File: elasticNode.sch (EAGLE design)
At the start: 113 parts, among them J1 ISP_CONN_6PIN, J10 ISP_CONN_6PIN, J2 FEMALE_HEADER_2X2, J3 FEMALE_HEADER_2X1, J4 FEMALE_HEADER_2X1, J5 FEMALE_HEADER_10X2, J8 USB_CONNSMT, J9 USB_CONNSMT, U1 ATMEGA64AQFN, U10 LTC3419DFN, U11 ATMEGA32U4, U2 SST26VF032B, U3 MRF24J40MA, U4 SPARTAN6-LX9, U5 SST26VF032B, U6 PAC1720, U7 PAC1720, U8 PAC1720, U9 FT232RSSOP28, X1 12MHz, X2 50MHz, X3 32MHz, X4 12MHz

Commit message: New layout is done
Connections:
- removed net N$33: U1.PB5_OC1A
- net 3V3: no longer R25.2
- net MCU_GPIO_0: now also J2.1, U1.PB7_OC2/OC1C; no longer J2.4, U1.PB6_OC1B
- net MCU_GPIO_1: now also J2.2, U1.PG3_TOSC2; no longer J2.3, U1.PE4_OC3B/INT4
- net MCU_GPIO_2: now also J2.3, U1.PG4_TOSC2; no longer J2.2, U1.PB7_OC2/OC1C
- net MCU_GPIO_3: now also J2.4, U1.PB6_OC1B; no longer J2.1, U1.PF0_ADC0
- net MCU_LED1: no longer U1.PB0_SS#
- net MCU_LED2: no longer U1.PE2_XCK0/AIN0
- net MCU_LED3: no longer U1.PE3_OC3A/AIN1
- net SDA: now also R25.2; no longer R25.1
- net WIRELESS_INT: now also U1.PF0_ADC0; no longer U1.PE7_ICP3/INT7
- net WIRELESS_RESET: now also U1.PB5_OC1A; no longer U1.PE5_OC3C/INT5
- net WIRELESS_WAKE: now also U1.PE2_XCK0/AIN0; no longer U1.PE6_T3/INT6
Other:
- moved on the sheet: R25
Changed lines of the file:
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@@
 <setting verticaltext="up"/>
 </settings>
-<grid distance="0.5" unitdist="mm" unit="mm" style="lines" multiple="1" display="yes" altdistance="0.01" altunitdist="inch" altunit="inch"/>
+<grid distance="1" unitdist="mm" unit="mm" style="lines" multiple="1" display="yes" altdistance="0.01" altunitdist="inch" altunit="inch"/>
 <layers>
 <layer number="1" name="Top" color="4" fill="1" visible="no" active="no"/>
@@
 </segment>
 <segment>
-<pinref part="U1" gate="G$1" pin="PE5_OC3C/INT5"/>
-<wire x1="7" y1="42" x2="7" y2="52" width="0.1524" layer="91"/>
-<label x="7" y="52" size="1.778" layer="95" rot="R90"/>
+<pinref part="U1" gate="G$1" pin="PB5_OC1A"/>
+<wire x1="-42" y1="-16" x2="-54" y2="-16" width="0.1524" layer="91"/>
+<label x="-54" y="-16" size="1.778" layer="95" rot="R180"/>
 </segment>
 </net>
@@
 </segment>
 <segment>
-<pinref part="U1" gate="G$1" pin="PE6_T3/INT6"/>
-<wire x1="4" y1="42" x2="4" y2="52" width="0.1524" layer="91"/>
-<label x="4" y="52" size="1.778" layer="95" rot="R90"/>
+<pinref part="U1" gate="G$1" pin="PE2_XCK0/AIN0"/>
+<wire x1="16" y1="52" x2="16" y2="42" width="0.1524" layer="91"/>
+<label x="16" y="52" size="1.778" layer="95" rot="R90"/>
 </segment>
 </net>
@@
 </segment>
 <segment>
-<pinref part="U1" gate="G$1" pin="PE7_ICP3/INT7"/>
-<wire x1="1" y1="42" x2="1" y2="52" width="0.1524" layer="91"/>
-<label x="1" y="52" size="1.778" layer="95" rot="R90"/>
+<pinref part="U1" gate="G$1" pin="PF0_ADC0"/>
+<wire x1="-2" y1="42" x2="-2" y2="52" width="0.1524" layer="91"/>
+<label x="-2" y="52" size="1.778" layer="95" rot="R90"/>
 </segment>
 </net>
@@
 <net name="MCU_GPIO_0" class="0">
 <segment>
+<pinref part="J2" gate="G$1" pin="1"/>
+<wire x1="134" y1="21.5" x2="122" y2="21.5" width="0.1524" layer="91"/>
+<label x="122" y="21.5" size="1.778" layer="95" rot="R180"/>
+</segment>
+<segment>
+<pinref part="U1" gate="G$1" pin="PB7_OC2/OC1C"/>
+<wire x1="-42" y1="-22" x2="-54" y2="-22" width="0.1524" layer="91"/>
+<label x="-54" y="-22" size="1.778" layer="95" rot="R180"/>
+</segment>
+</net>
+<net name="MCU_GPIO_1" class="0">
+<segment>
+<pinref part="J2" gate="G$1" pin="2"/>
+<wire x1="134" y1="18.5" x2="122" y2="18.5" width="0.1524" layer="91"/>
+<label x="122" y="18.5" size="1.778" layer="95" rot="R180"/>
+</segment>
+<segment>
+<pinref part="U1" gate="G$1" pin="PG3_TOSC2"/>
+<wire x1="54" y1="-13" x2="42" y2="-13" width="0.1524" layer="91"/>
+<label x="54" y="-13" size="1.778" layer="95"/>
+</segment>
+</net>
+<net name="MCU_GPIO_2" class="0">
+<segment>
+<pinref part="J2" gate="G$1" pin="3"/>
+<wire x1="154" y1="18.5" x2="165.5" y2="18.5" width="0.1524" layer="91"/>
+<label x="165.5" y="18.5" size="1.778" layer="95"/>
+</segment>
+<segment>
+<pinref part="U1" gate="G$1" pin="PG4_TOSC2"/>
+<wire x1="42" y1="-10" x2="54" y2="-10" width="0.1524" layer="91"/>
+<label x="54" y="-10" size="1.778" layer="95"/>
+</segment>
+</net>
+<net name="MCU_GPIO_3" class="0">
+<segment>
 <pinref part="J2" gate="G$1" pin="4"/>
 <wire x1="154" y1="21.5" x2="165.5" y2="21.5" width="0.1524" layer="91"/>
@@
 </segment>
 </net>
-<net name="MCU_GPIO_1" class="0">
-<segment>
-<pinref part="J2" gate="G$1" pin="3"/>
-<wire x1="154" y1="18.5" x2="165.5" y2="18.5" width="0.1524" layer="91"/>
-<label x="165.5" y="18.5" size="1.778" layer="95"/>
-</segment>
-<segment>
-<pinref part="U1" gate="G$1" pin="PE4_OC3B/INT4"/>
-<wire x1="10" y1="42" x2="10" y2="52" width="0.1524" layer="91"/>
-<label x="10" y="52" size="1.778" layer="95" rot="R90"/>
-</segment>
-</net>
-<net name="MCU_GPIO_2" class="0">
-<segment>
-<pinref part="J2" gate="G$1" pin="2"/>
-<wire x1="134" y1="18.5" x2="122" y2="18.5" width="0.1524" layer="91"/>
-<label x="122" y="18.5" size="1.778" layer="95" rot="R180"/>
-</segment>
-<segment>
-<pinref part="U1" gate="G$1" pin="PB7_OC2/OC1C"/>
-<wire x1="-42" y1="-22" x2="-54" y2="-22" width="0.1524" layer="91"/>
-<label x="-54" y="-22" size="1.778" layer="95" rot="R180"/>
-</segment>
-</net>
-<net name="MCU_GPIO_3" class="0">
-<segment>
-<pinref part="U1" gate="G$1" pin="PF0_ADC0"/>
-<wire x1="-2" y1="42" x2="-2" y2="52" width="0.1524" layer="91"/>
-<label x="-2" y="52" size="1.778" layer="95" rot="R90"/>
-</segment>
-<segment>
-<pinref part="J2" gate="G$1" pin="1"/>
-<wire x1="134" y1="21.5" x2="122" y2="21.5" width="0.1524" layer="91"/>
-<label x="122" y="21.5" size="1.778" layer="95" rot="R180"/>
-</segment>
-</net>
 <net name="N$13" class="0">
 <segment>
@@
 </segment>
 <segment>
-<pinref part="U1" gate="G$1" pin="PB0_SS#"/>
-<wire x1="-42" y1="-1" x2="-54" y2="-1" width="0.1524" layer="91"/>
-<label x="-54" y="-1" size="1.778" layer="95" rot="R180"/>
-</segment>
-<segment>
 <pinref part="U1" gate="G$1" pin="PD6_T1"/>
 <wire x1="19" y1="-40" x2="19" y2="-50" width="0.1524" layer="91"/>
@@
 </segment>
 <segment>
-<pinref part="U1" gate="G$1" pin="PE2_XCK0/AIN0"/>
-<wire x1="16" y1="52" x2="16" y2="42" width="0.1524" layer="91"/>
-<label x="16" y="52" size="1.778" layer="95" rot="R90"/>
-</segment>
-<segment>
 <pinref part="U1" gate="G$1" pin="PD5_XCK1"/>
 <wire x1="16" y1="-40" x2="16" y2="-50" width="0.1524" layer="91"/>
@@
 <wire x1="138.54" y1="-17" x2="129" y2="-17" width="0.1524" layer="91"/>
 <label x="129" y="-17" size="1.778" layer="95" rot="R180"/>
-</segment>
-<segment>
-<pinref part="U1" gate="G$1" pin="PE3_OC3A/AIN1"/>
-<wire x1="13" y1="42" x2="13" y2="52" width="0.1524" layer="91"/>
-<label x="13" y="52" size="1.778" layer="95" rot="R90"/>
 </segment>
 <segment>
@@
 <wire x1="42" y1="-16" x2="54" y2="-16" width="0.1524" layer="91"/>
 <label x="54" y="-16" size="1.778" layer="95"/>
-</segment>
-</net>
-<net name="N$33" class="0">
-<segment>
-<pinref part="U1" gate="G$1" pin="PB5_OC1A"/>
-<wire x1="-42" y1="-16" x2="-54" y2="-16" width="0.1524" layer="91"/>
-<label x="-54" y="-16" size="1.778" layer="95" rot="R180"/>
 </segment>
 </net>
@@
 <instance part="R22" gate="G$1" x="-40" y="-105" rot="R90"/>
 <instance part="R24" gate="G$1" x="26" y="-94.5" rot="R90"/>
-<instance part="R25" gate="G$1" x="26" y="-112.5" rot="R270"/>
+<instance part="R25" gate="G$1" x="26" y="-112.5" rot="R90"/>
 <instance part="U6" gate="G$1" x="-1" y="-52"/>
 <instance part="R20" gate="G$1" x="21" y="-67" rot="R90"/>
@@
 </segment>
 <segment>
-<pinref part="R25" gate="G$1" pin="2"/>
+<label x="26" y="-129" size="1.778" layer="95" rot="R270"/>
 <wire x1="26" y1="-116.96" x2="26" y2="-129" width="0.1524" layer="91"/>
-<label x="26" y="-129" size="1.778" layer="95" rot="R270"/>
 </segment>
 <segment>
@@
 <wire x1="16" y1="-107" x2="26" y2="-107" width="0.1524" layer="91"/>
 <label x="30" y="-107" size="1.778" layer="95"/>
-<pinref part="R25" gate="G$1" pin="1"/>
+<pinref part="R25" gate="G$1" pin="2"/>
 <wire x1="26" y1="-107" x2="30" y2="-107" width="0.1524" layer="91"/>
-<wire x1="26" y1="-108.04" x2="26" y2="-107" width="0.1524" layer="91"/>
+<wire x1="26" y1="-107" x2="26" y2="-108.04" width="0.1524" layer="91"/>
 <junction x="26" y="-107"/>
 </segment>

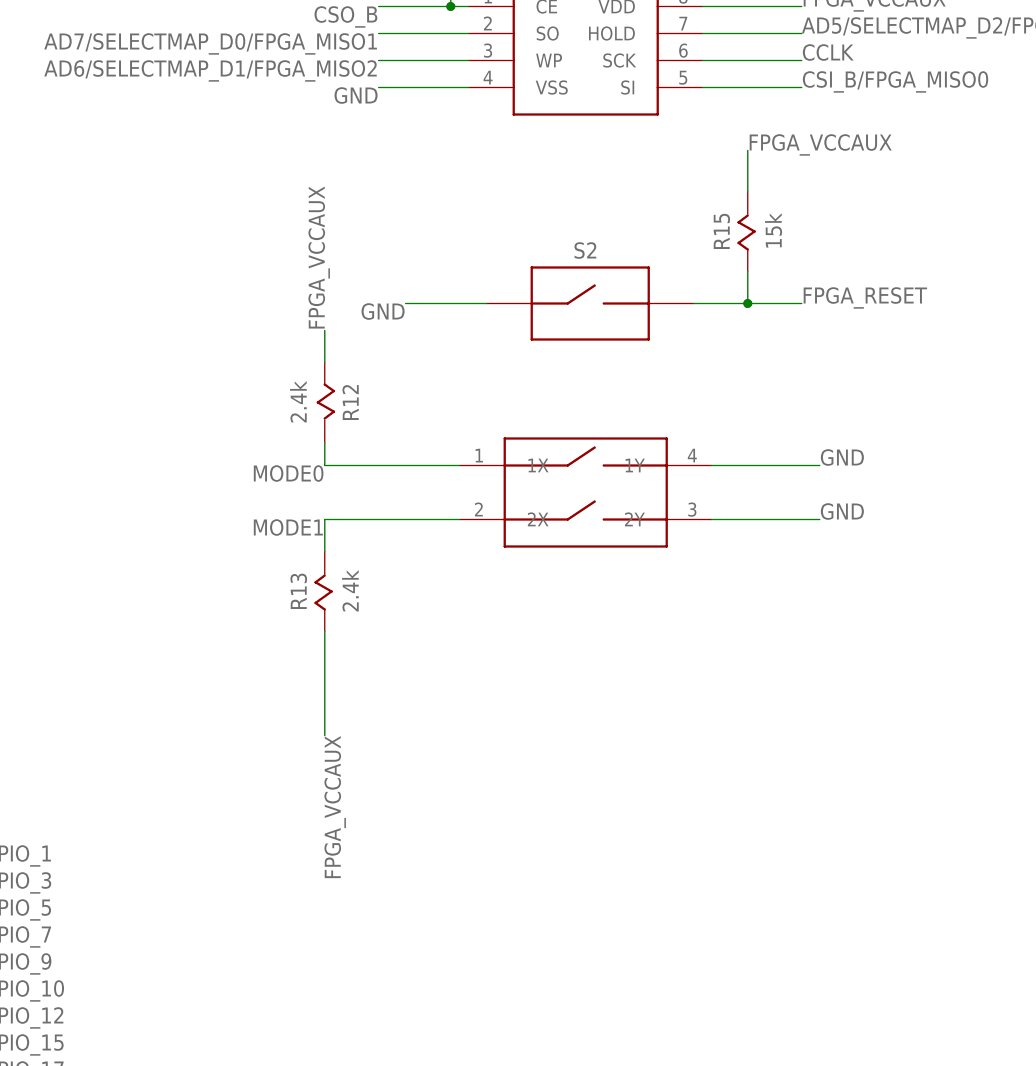
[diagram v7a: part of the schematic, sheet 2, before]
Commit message: 4-switch dip added into design
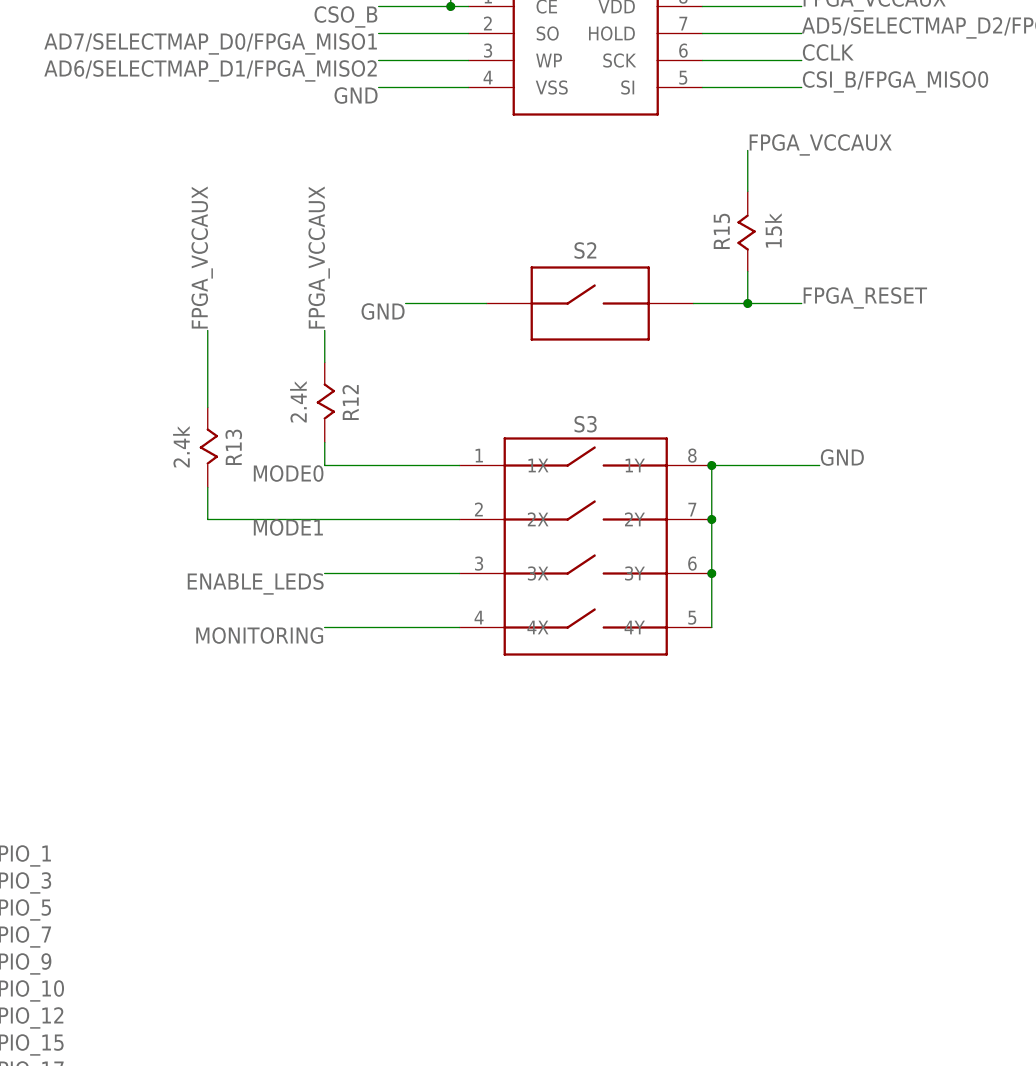
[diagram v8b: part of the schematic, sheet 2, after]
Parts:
- S3: value SPST_DIP_2SMT -> SPST_DIP_4; device connectors:SPST_DIP_2SMT -> connectors:SPST_DIP_4
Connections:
- new net ENABLE_LEDS: S3.3X, U1.PE7_ICP3/INT7
- new net MONITORING: S3.4X, U11.PE6(INT6/AIN0)
- net GND: now also S3.3Y, S3.4Y
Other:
- moved on the sheet: R13
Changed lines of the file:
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@@
 <attribute name="SPICEPREFIX" value="X"/>
 </part>
-<part name="S3" library="connectors" deviceset="SPST_DIP_2" device="SMT"/>
 <part name="R12" library="passive" deviceset="RESISTOR" device="" value="2.4k"/>
 <part name="R13" library="passive" deviceset="RESISTOR" device="" value="2.4k"/>
@@
 <part name="R36" library="passive" deviceset="RESISTOR" device="" value=".8"/>
 <part name="J5" library="connectors" deviceset="FEMALE_HEADER_10X2" device=""/>
+<part name="S3" library="connectors" deviceset="SPST_DIP_4" device=""/>
 </parts>
 <sheets>
@@
 <wire x1="42" y1="-16" x2="54" y2="-16" width="0.1524" layer="91"/>
 <label x="54" y="-16" size="1.778" layer="95"/>
+</segment>
+</net>
+<net name="ENABLE_LEDS" class="0">
+<segment>
+<pinref part="U1" gate="G$1" pin="PE7_ICP3/INT7"/>
+<wire x1="1" y1="42" x2="1" y2="52" width="0.1524" layer="91"/>
+<label x="1" y="52" size="1.778" layer="95" rot="R90"/>
 </segment>
 </net>
@@
 <instance part="S2" gate="G$1" x="197" y="-82"/>
 <instance part="R15" gate="G$1" x="215" y="-74" rot="R90"/>
-<instance part="S3" gate="G$1" x="197" y="-103"/>
 <instance part="R12" gate="G$1" x="168" y="-93" rot="R270"/>
-<instance part="R13" gate="G$1" x="168" y="-114" rot="R90"/>
+<instance part="R13" gate="G$1" x="155" y="-98" rot="R270"/>
 <instance part="J4" gate="G$1" x="104" y="-75.5"/>
 <instance part="J3" gate="G$1" x="104" y="-60"/>
@@
 <instance part="R14" gate="G$1" x="182" y="-41" rot="R270"/>
 <instance part="J5" gate="G$1" x="104" y="-157"/>
+<instance part="S3" gate="G$1" x="197" y="-109"/>
 </instances>
 <busses>
@@
 </segment>
 <segment>
-<pinref part="S3" gate="G$1" pin="1Y"/>
+<pinref part="S3" gate="G$1" pin="2Y"/>
 <wire x1="211" y1="-100" x2="223" y2="-100" width="0.1524" layer="91"/>
 <label x="223" y="-100" size="1.778" layer="95"/>
-</segment>
-<segment>
-<pinref part="S3" gate="G$1" pin="2Y"/>
-<wire x1="211" y1="-106" x2="223" y2="-106" width="0.1524" layer="91"/>
-<label x="223" y="-106" size="1.778" layer="95"/>
+<wire x1="211" y1="-106" x2="211" y2="-100" width="0.1524" layer="91"/>
+<pinref part="S3" gate="G$1" pin="1Y"/>
+<junction x="211" y="-100"/>
+<pinref part="S3" gate="G$1" pin="4Y"/>
+<pinref part="S3" gate="G$1" pin="3Y"/>
+<wire x1="211" y1="-118" x2="211" y2="-112" width="0.1524" layer="91"/>
+<wire x1="211" y1="-112" x2="211" y2="-106" width="0.1524" layer="91"/>
+<junction x="211" y="-112"/>
+<junction x="211" y="-106"/>
 </segment>
 <segment>
@@
 <segment>
 <pinref part="R13" gate="G$1" pin="1"/>
-<wire x1="168" y1="-118.46" x2="168" y2="-130" width="0.1524" layer="91"/>
-<label x="168" y="-130" size="1.778" layer="95" rot="R270"/>
+<wire x1="155" y1="-93.54" x2="155" y2="-85" width="0.1524" layer="91"/>
+<label x="155" y="-85" size="1.778" layer="95" rot="R90"/>
 </segment>
 <segment>
@@
 </segment>
 <segment>
-<pinref part="S3" gate="G$1" pin="1X"/>
 <wire x1="183" y1="-100" x2="168" y2="-100" width="0.1524" layer="91"/>
 <pinref part="R12" gate="G$1" pin="2"/>
 <wire x1="168" y1="-100" x2="168" y2="-97.46" width="0.1524" layer="91"/>
 <label x="168" y="-100" size="1.778" layer="95" rot="R180"/>
+<pinref part="S3" gate="G$1" pin="1X"/>
 </segment>
 </net>
@@
 </segment>
 <segment>
-<pinref part="S3" gate="G$1" pin="2X"/>
-<wire x1="183" y1="-106" x2="168" y2="-106" width="0.1524" layer="91"/>
+<wire x1="183" y1="-106" x2="155" y2="-106" width="0.1524" layer="91"/>
 <label x="168" y="-106" size="1.778" layer="95" rot="R180"/>
 <pinref part="R13" gate="G$1" pin="2"/>
-<wire x1="168" y1="-109.54" x2="168" y2="-106" width="0.1524" layer="91"/>
+<wire x1="155" y1="-102.46" x2="155" y2="-106" width="0.1524" layer="91"/>
+<pinref part="S3" gate="G$1" pin="2X"/>
 </segment>
 </net>
@@
 <wire x1="1.5" y1="79" x2="1.5" y2="69.5" width="0.1524" layer="91"/>
 <label x="1.5" y="79" size="1.778" layer="95" rot="R90"/>
+</segment>
+</net>
+<net name="ENABLE_LEDS" class="0">
+<segment>
+<pinref part="S3" gate="G$1" pin="3X"/>
+<wire x1="183" y1="-112" x2="168" y2="-112" width="0.1524" layer="91"/>
+<label x="168" y="-112" size="1.778" layer="95" rot="R180"/>
+</segment>
+</net>
+<net name="MONITORING" class="0">
+<segment>
+<pinref part="S3" gate="G$1" pin="4X"/>
+<wire x1="183" y1="-118" x2="168" y2="-118" width="0.1524" layer="91"/>
+<label x="168" y="-118" size="1.778" layer="95" rot="R180"/>
 </segment>
 </net>
@@
 </segment>
 </net>
+<net name="MONITORING" class="0">
+<segment>
+<pinref part="U11" gate="G$1" pin="PE6(INT6/AIN0)"/>
+<wire x1="168" y1="-139" x2="168" y2="-149" width="0.1524" layer="91"/>
+<label x="168" y="-149" size="1.778" layer="95" rot="R270"/>
+</segment>
+</net>
